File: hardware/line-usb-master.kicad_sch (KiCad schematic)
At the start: 109 parts, among them J1 USB_B, J2 Conn_01x02, J3 Banana, J4 Conn_01x01, J5 Conn_01x01, J6 Conn_01x01, Q6 2N7002, SW1 SW_SPDT, SW2 SW_SPDT, SW3 SW_SPDT, SW4 TVCM17015BPB, U1 TPS61085, U3 FT4232H, U4 MCP2003, U5 93LCxxC, U6 MCP2003, U7 74HCT595, U8 LMR51420, Y1 CFPX-104

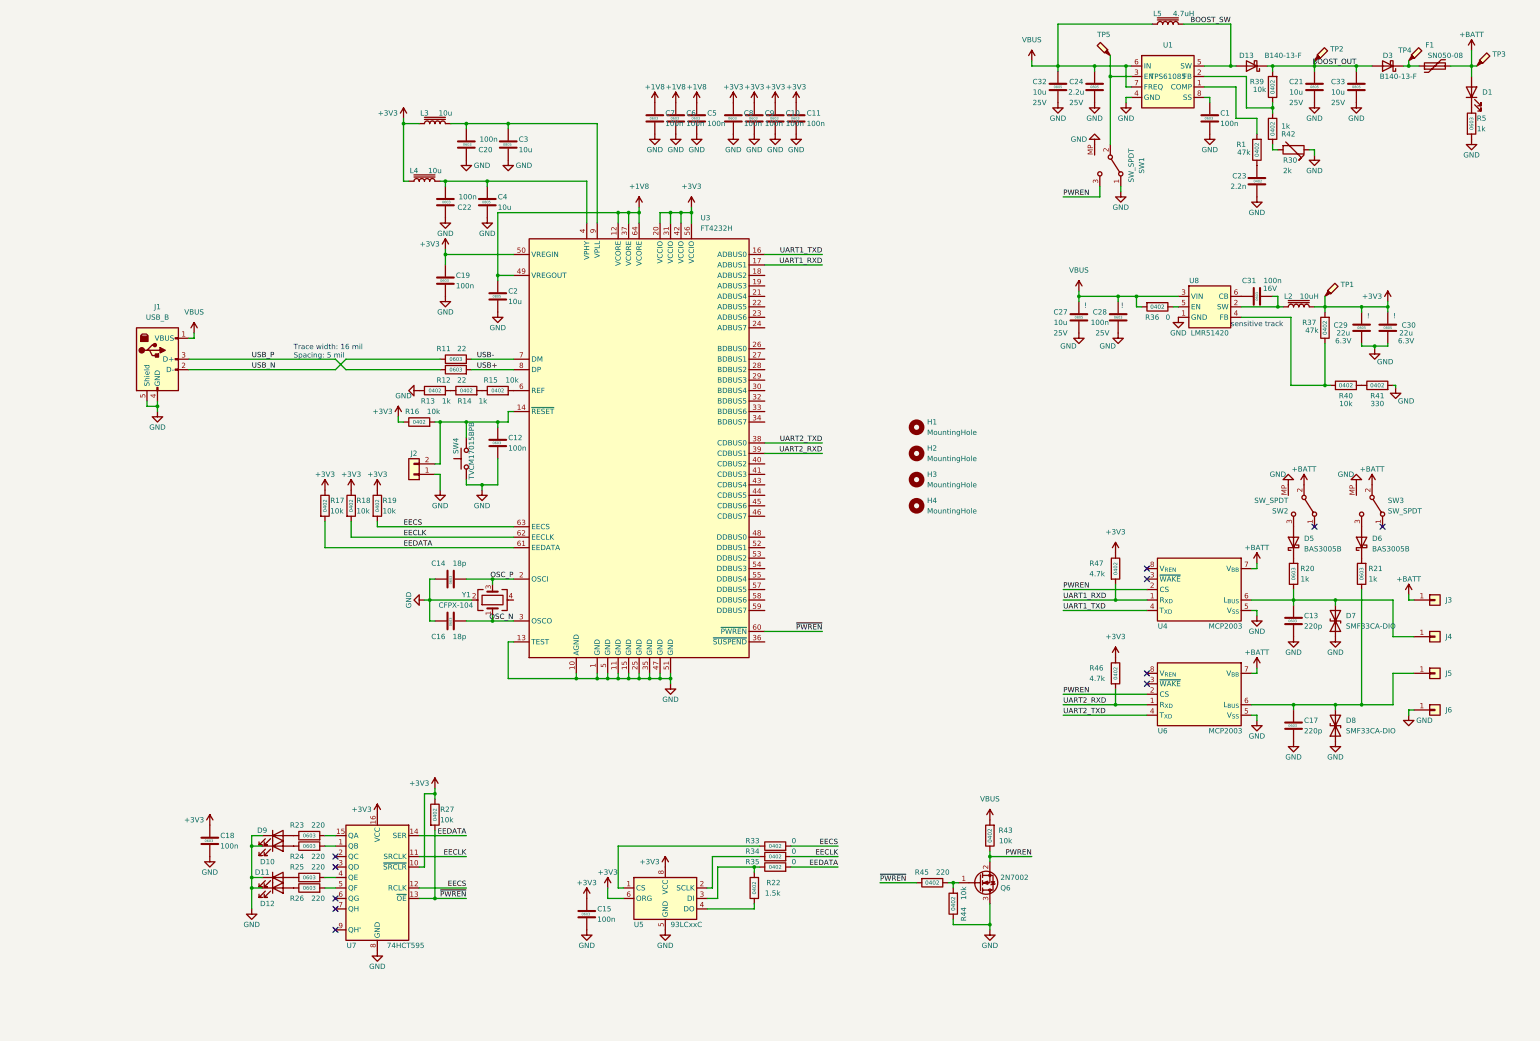
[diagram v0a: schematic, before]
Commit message: Hardware fixes
Crystal 4th pin connected to GND
Removed series resistor from USB lines
Corrected pullup on EEPROM lines
Fixes PWREN Mosfet orientation
Added fiducial
Added 4 pin connectors for direct wired variant
Increased pad size of the front panel switches
Added 3d model to shift register
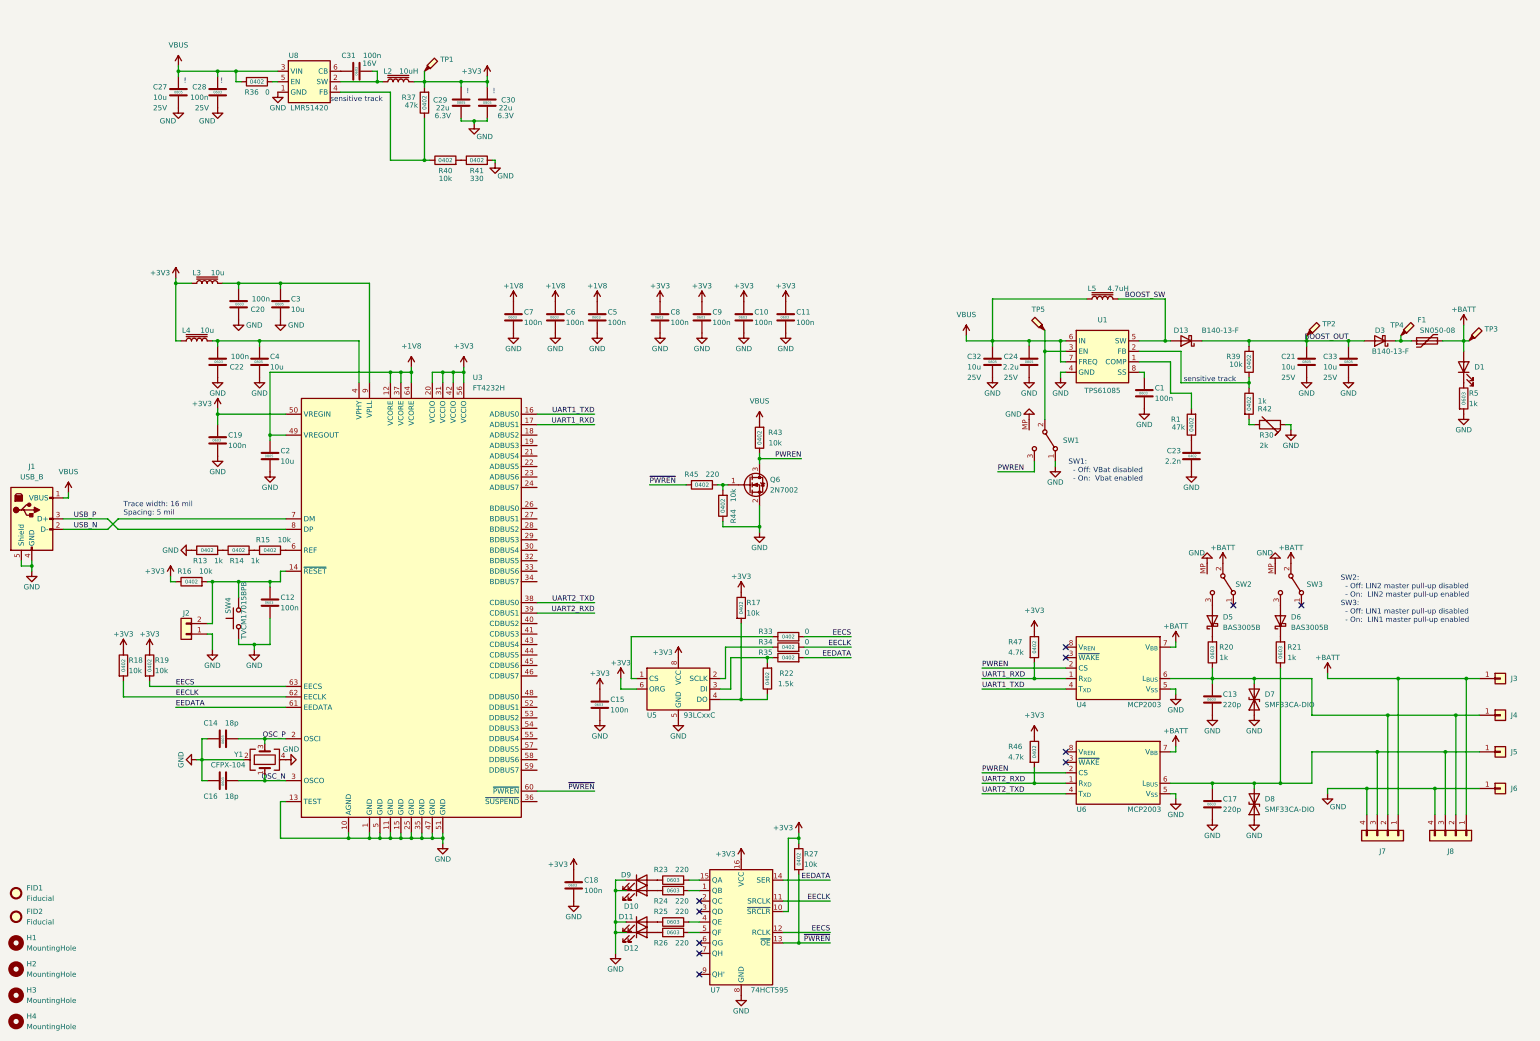
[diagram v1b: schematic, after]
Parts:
- removed R11, R12: 22, Resistor_SMD:R_0603_1608Metric, symbol Device:R
- added FID1, FID2: Fiducial, Fiducial:Fiducial_1mm_Mask2mm, symbol Mechanical:Fiducial
- added J7, J8: Conn_01x04, Connector_PinHeader_2.54mm:PinHeader_1x04_P2.54mm_Vertical, symbol Connector_Generic:Conn_01x04
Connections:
- net USB+ is gone; now on net USB_P: U3.8 (DP)
- net USB- is gone; now on net USB_N: U3.7 (DM)
- net +BATT: now also J7.1 (Pin_1), J8.1 (Pin_1)
- net EEDATA: no longer R17.2
- net GND: now also Q6.2 (S), Y1.4, J7.4 (Pin_4), J8.4 (Pin_4); no longer Q6.3 (D)
- net PWREN: now also Q6.3 (D); no longer Q6.2 (S)
- net at C13.1, D7.2 (A2), J4.1 (Pin_1)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: now also J7.2 (Pin_2), J8.2 (Pin_2)
- net at C17.1, D8.2 (A2), J5.1 (Pin_1)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: now also J7.3 (Pin_3), J8.3 (Pin_3)
- net at R22.1, U5.4 (DO): now also R17.2
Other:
- note added: "SW1: - Off: VBat disabled - On: Vbat enabled"
- note added: "SW2: - Off: LIN2 master pull-up disabled - On: LIN2 master pull-up enabled SW3: - Off: LIN1 master pull-up disabled - On: LIN1 master pull-up enabled"
- moved on the sheet: C1, C10, C11, C12, C13, C14, C15, C16, C17, C18, C19, C2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
